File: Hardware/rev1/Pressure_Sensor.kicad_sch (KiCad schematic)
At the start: 4 parts, among them U3 MS5607-02BA

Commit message: Add buses (maybe)
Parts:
- added J1: Conn_ARM_JTAG_SWD_10, symbol Connector:Conn_ARM_JTAG_SWD_10
- added U1: W25Q128JVS, Package_SO:SOIC-8_5.23x5.23mm_P1.27mm, symbol Memory_Flash:W25Q128JVS
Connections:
- net +3.3V: now also J1.1 (VTref), U1.8 (VCC)
- net GND: now also J1.3 (GND), J1.5 (GND), J1.9 (GNDDetect), U1.4 (GND)
- new net JTCK/SWCLK: J1.4 (SWCLK/TCK)
- new net JTDI/NC: J1.8 (NC/TDI)
- new net JTDO/SWO: J1.6 (SWO/TDO)
- new net NRESET: J1.10 (~{RESET})
- new net SPI1_MISO: U1.2 (DO(IO1))
- new net SPI1_MOSI: U1.5 (DI(IO0))
- new net SPI_CLK: U1.6 (CLK)
- new net TMS/SWDIO: J1.2 (SWDIO/TMS)
- no-connect marks 1 -> 4
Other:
- moved on the sheet: C11, R6, R7, U3

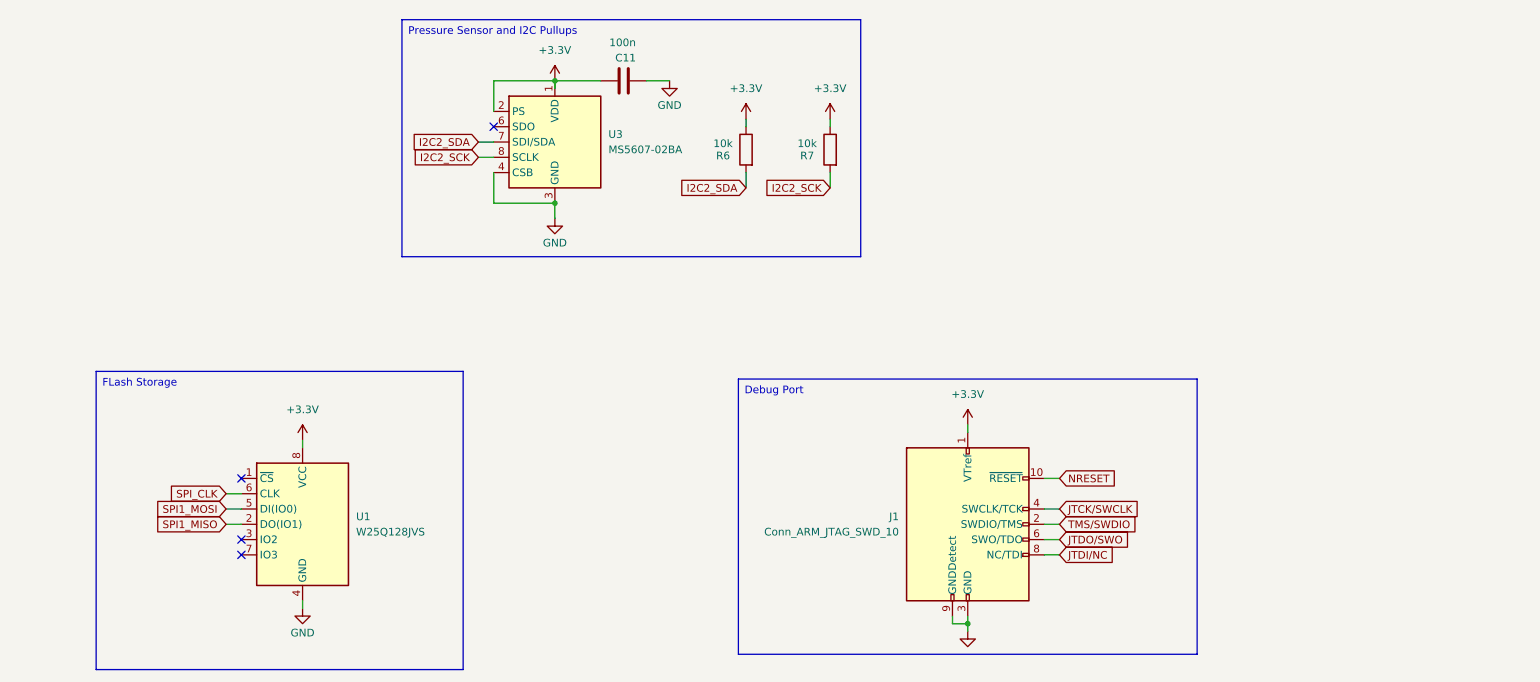
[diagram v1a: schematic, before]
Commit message: Removed backup files and folder as redundant on GitHub, updated hierarchical labels to include NRESET
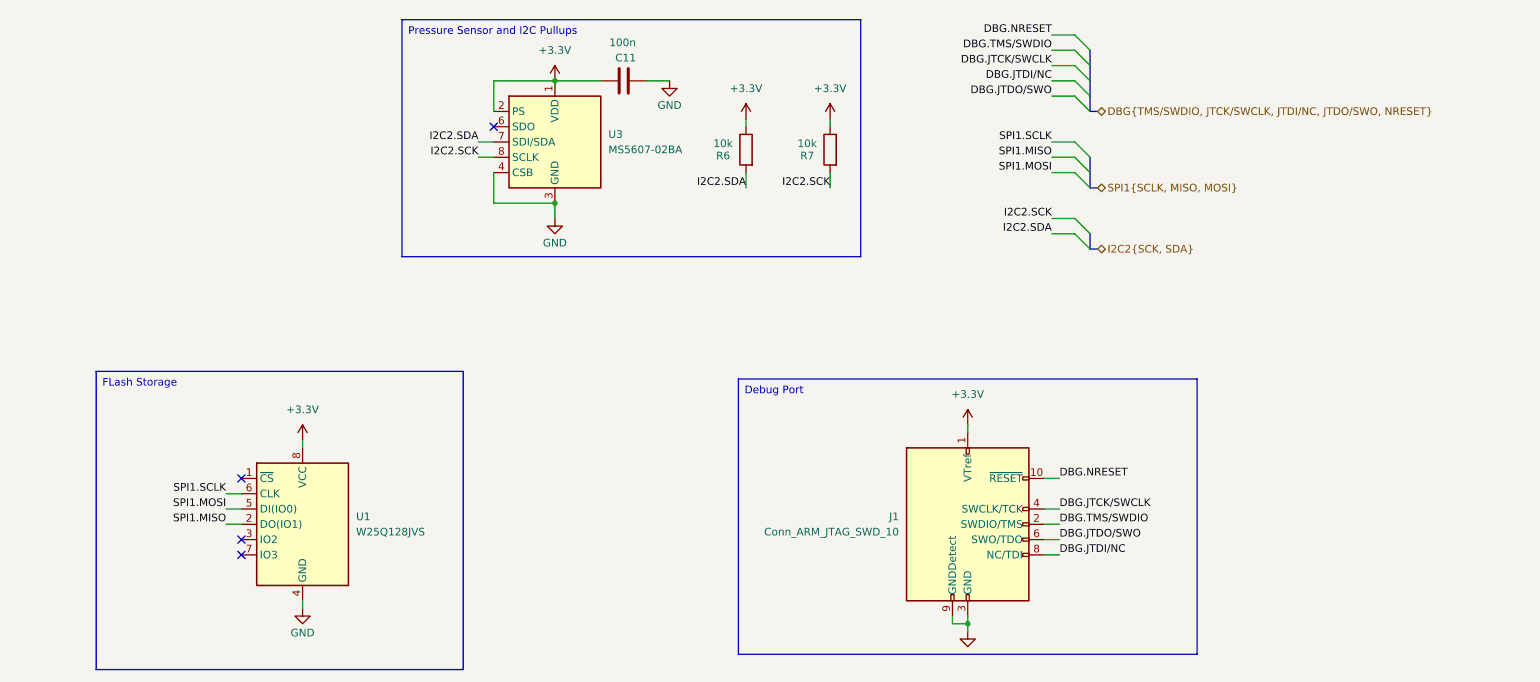
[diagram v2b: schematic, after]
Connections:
- net I2C2_SCK renamed I2C2.SCK
- net I2C2_SDA renamed I2C2.SDA
- net JTCK/SWCLK renamed DBG.JTCK/SWCLK
- net JTDI/NC renamed DBG.JTDI/NC
- net JTDO/SWO renamed DBG.JTDO/SWO
- net NRESET renamed DBG.NRESET
- net SPI1_MISO renamed SPI1.MISO
- net SPI1_MOSI renamed SPI1.MOSI
- net SPI_CLK renamed SPI1.SCLK
- net TMS/SWDIO renamed DBG.TMS/SWDIO

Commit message: Updated footprints for capacitors
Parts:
- C11: footprint (none) -> Capacitor_SMD:C_0603_1608Metric
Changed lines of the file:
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@@
 			)
 		)
-		(property "Footprint" ""
+		(property "Footprint" "Capacitor_SMD:C_0603_1608Metric"
 			(at 151.13 46.0248 0)
 			(effects

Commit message: Revert "Updated footprints for capacitors"
This reverts commit 54b9e5590742c75ae1802e9536bdc0a5b115109b.
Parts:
- C11: footprint Capacitor_SMD:C_0603_1608Metric -> (none)
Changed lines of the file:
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@@
 			)
 		)
-		(property "Footprint" "Capacitor_SMD:C_0603_1608Metric"
+		(property "Footprint" ""
 			(at 151.13 46.0248 0)
 			(effects

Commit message: Finish schematics, assign footprints
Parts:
- C11: footprint (none) -> Capacitor_SMD:C_0402_1005Metric
- J1: footprint (none) -> Connector_PinHeader_1.27mm:PinHeader_2x05_P1.27mm_Horizontal
- R6, R7: footprint Resistor_SMD:R_0402_1005Metric -> Resistor_SMD:R_0603_1608Metric
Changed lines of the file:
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@@
 			)
 		)
-		(property "Footprint" "Resistor_SMD:R_0402_1005Metric"
+		(property "Footprint" "Resistor_SMD:R_0603_1608Metric"
 			(at 183.388 58.42 90)
 			(effects
@@
 			)
 		)
-		(property "Footprint" ""
+		(property "Footprint" "Capacitor_SMD:C_0402_1005Metric"
 			(at 151.13 46.0248 0)
 			(effects
@@
 			)
 		)
-		(property "Footprint" "Resistor_SMD:R_0402_1005Metric"
+		(property "Footprint" "Resistor_SMD:R_0603_1608Metric"
 			(at 169.418 58.42 90)
 			(effects
@@
 			)
 		)
-		(property "Footprint" ""
+		(property "Footprint" "Connector_PinHeader_1.27mm:PinHeader_2x05_P1.27mm_Horizontal"
 			(at 204.47 120.65 0)
 			(effects

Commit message: Revert "Merge remote-tracking branch 'origin/dev'"
This reverts commit 9d6b38d1428df59ab2602e839e1db75647d3fbc2, reversing
changes made to aa461fd2fa90bcdcb689545e3dbed326723346fe.
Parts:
- C11: footprint Capacitor_SMD:C_0402_1005Metric -> (none)
- J1: footprint Connector_PinHeader_1.27mm:PinHeader_2x05_P1.27mm_Horizontal -> (none)
- R6, R7: footprint Resistor_SMD:R_0603_1608Metric -> Resistor_SMD:R_0402_1005Metric
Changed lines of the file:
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@@
 			)
 		)
-		(property "Footprint" "Resistor_SMD:R_0603_1608Metric"
+		(property "Footprint" "Resistor_SMD:R_0402_1005Metric"
 			(at 183.388 58.42 90)
 			(effects
@@
 			)
 		)
-		(property "Footprint" "Capacitor_SMD:C_0402_1005Metric"
+		(property "Footprint" ""
 			(at 151.13 46.0248 0)
 			(effects
@@
 			)
 		)
-		(property "Footprint" "Resistor_SMD:R_0603_1608Metric"
+		(property "Footprint" "Resistor_SMD:R_0402_1005Metric"
 			(at 169.418 58.42 90)
 			(effects
@@
 			)
 		)
-		(property "Footprint" "Connector_PinHeader_1.27mm:PinHeader_2x05_P1.27mm_Horizontal"
+		(property "Footprint" ""
 			(at 204.47 120.65 0)
 			(effects

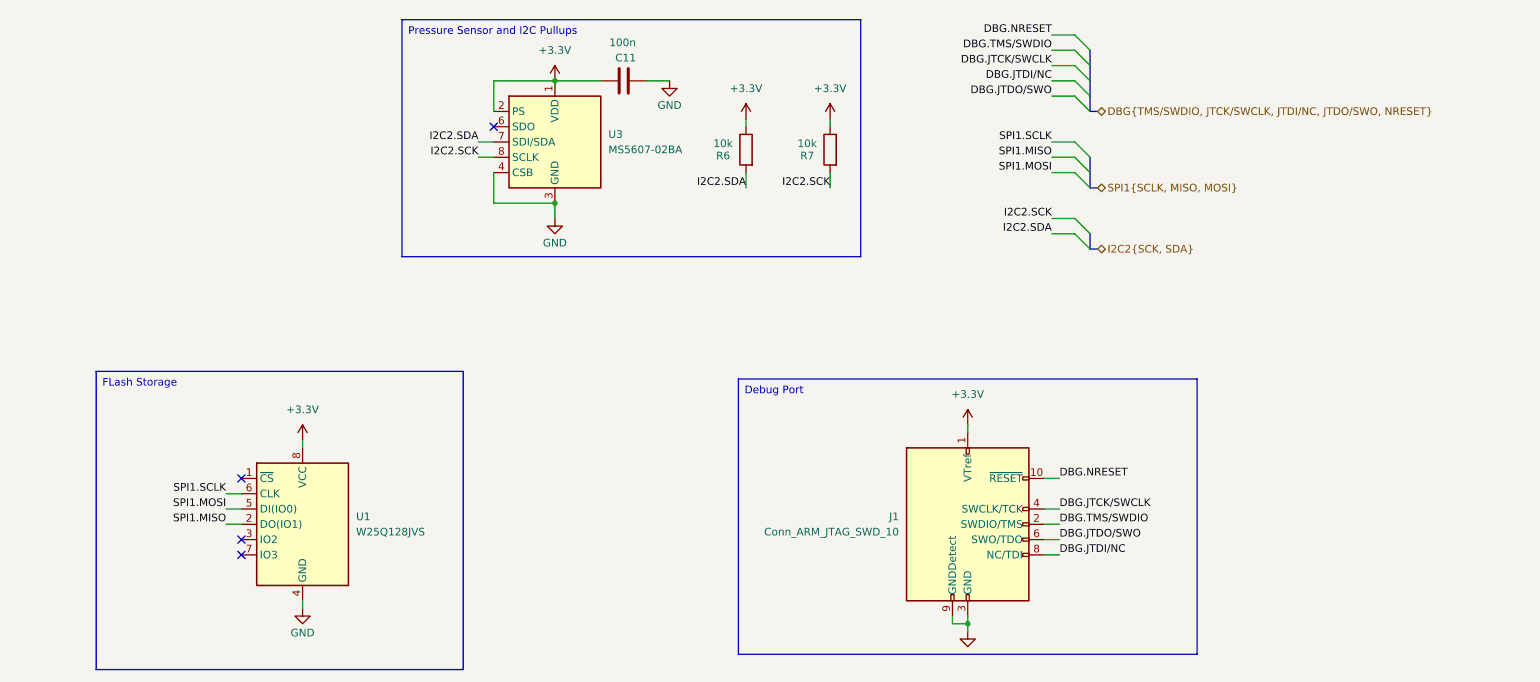
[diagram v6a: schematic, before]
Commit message: GitHub Shenanegans - Taken things from Shon's commit because easier to fix that way than to figure out how to merge properly
Literally for the buzzer and switch, hopefully retain the capacitor fix
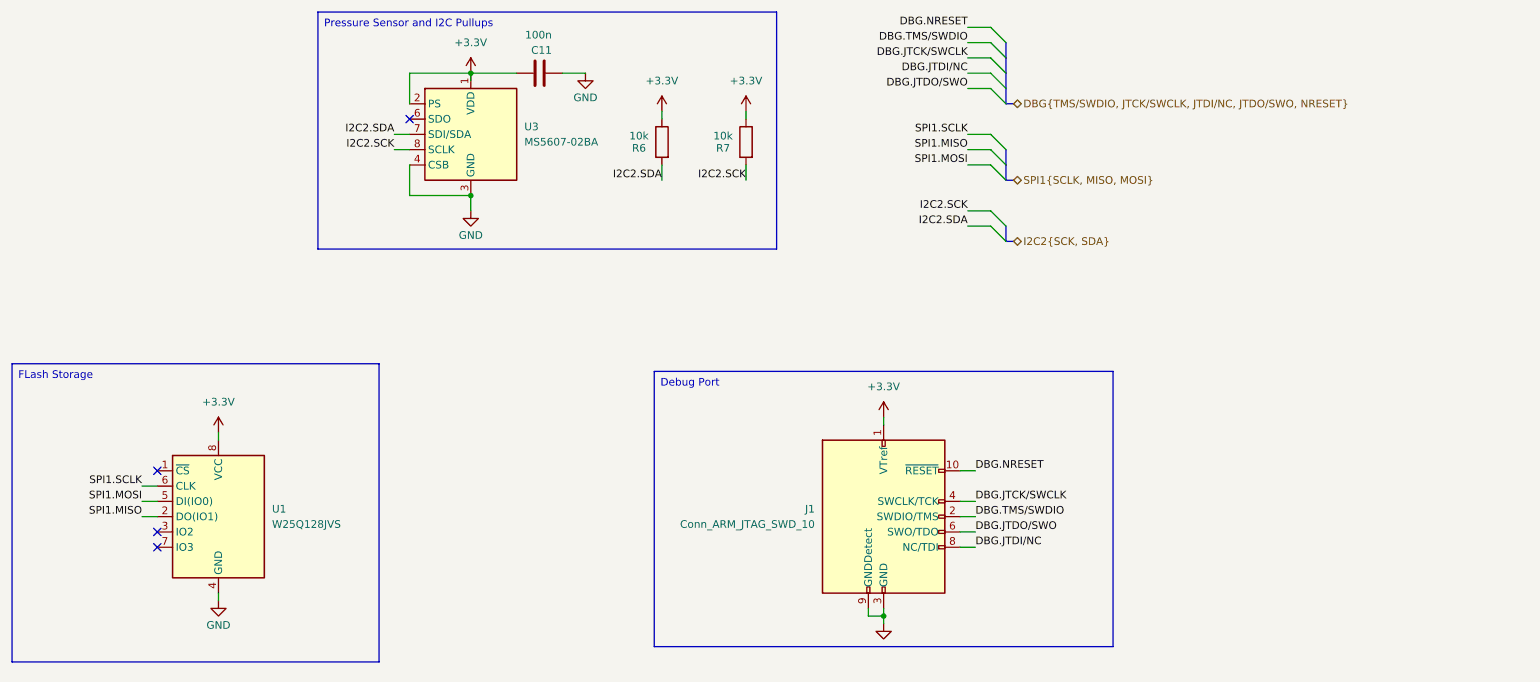
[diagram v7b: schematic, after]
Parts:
- C11: footprint (none) -> Capacitor_SMD:C_0402_1005Metric
- J1: footprint (none) -> Connector_PinHeader_1.27mm:PinHeader_2x05_P1.27mm_Horizontal
- R6, R7: footprint Resistor_SMD:R_0402_1005Metric -> Resistor_SMD:R_0603_1608Metric

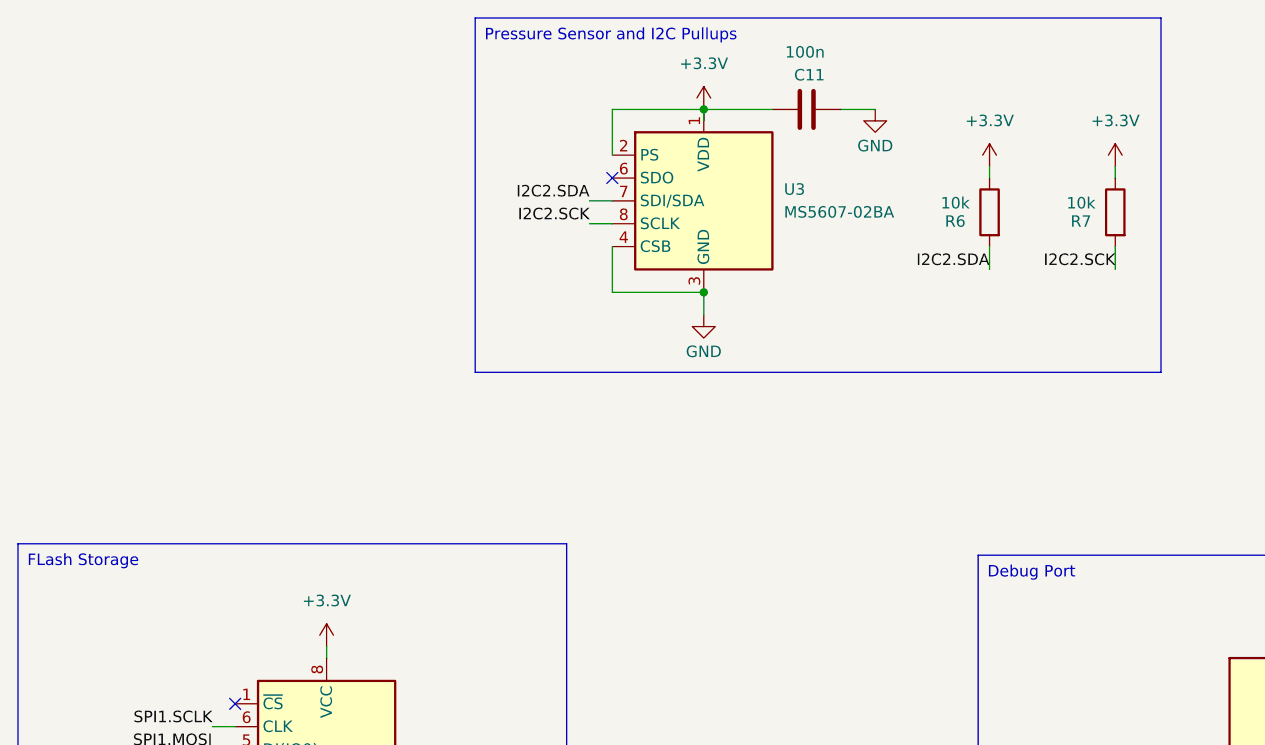
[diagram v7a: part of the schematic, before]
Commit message: Updated traces, moved mounting hole, selected switching diodes for power regulation
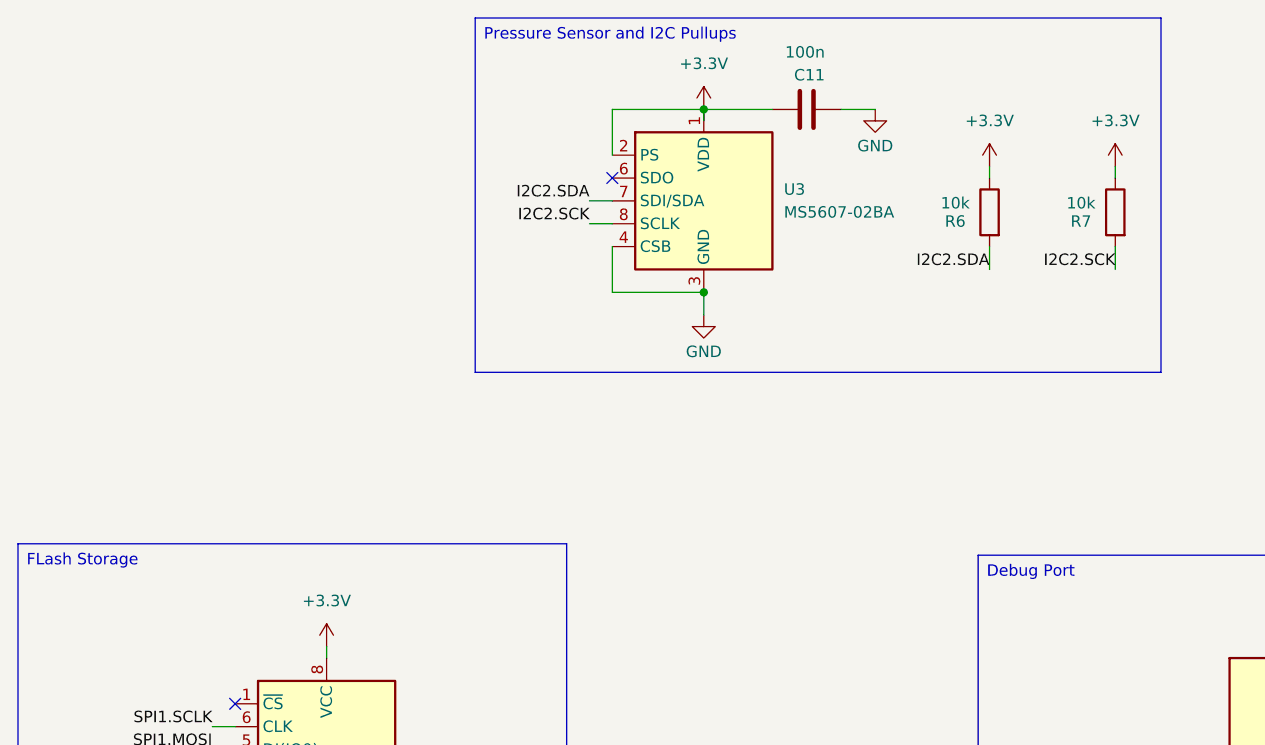
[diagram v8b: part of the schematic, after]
